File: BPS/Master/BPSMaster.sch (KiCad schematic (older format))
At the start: 21 parts, among them J1 SWD, J12 Logic Analyzer, J13 CAN Analyzer, SW1 B3SL-1002P, U1 STM32F413RHTx, Y1 8M

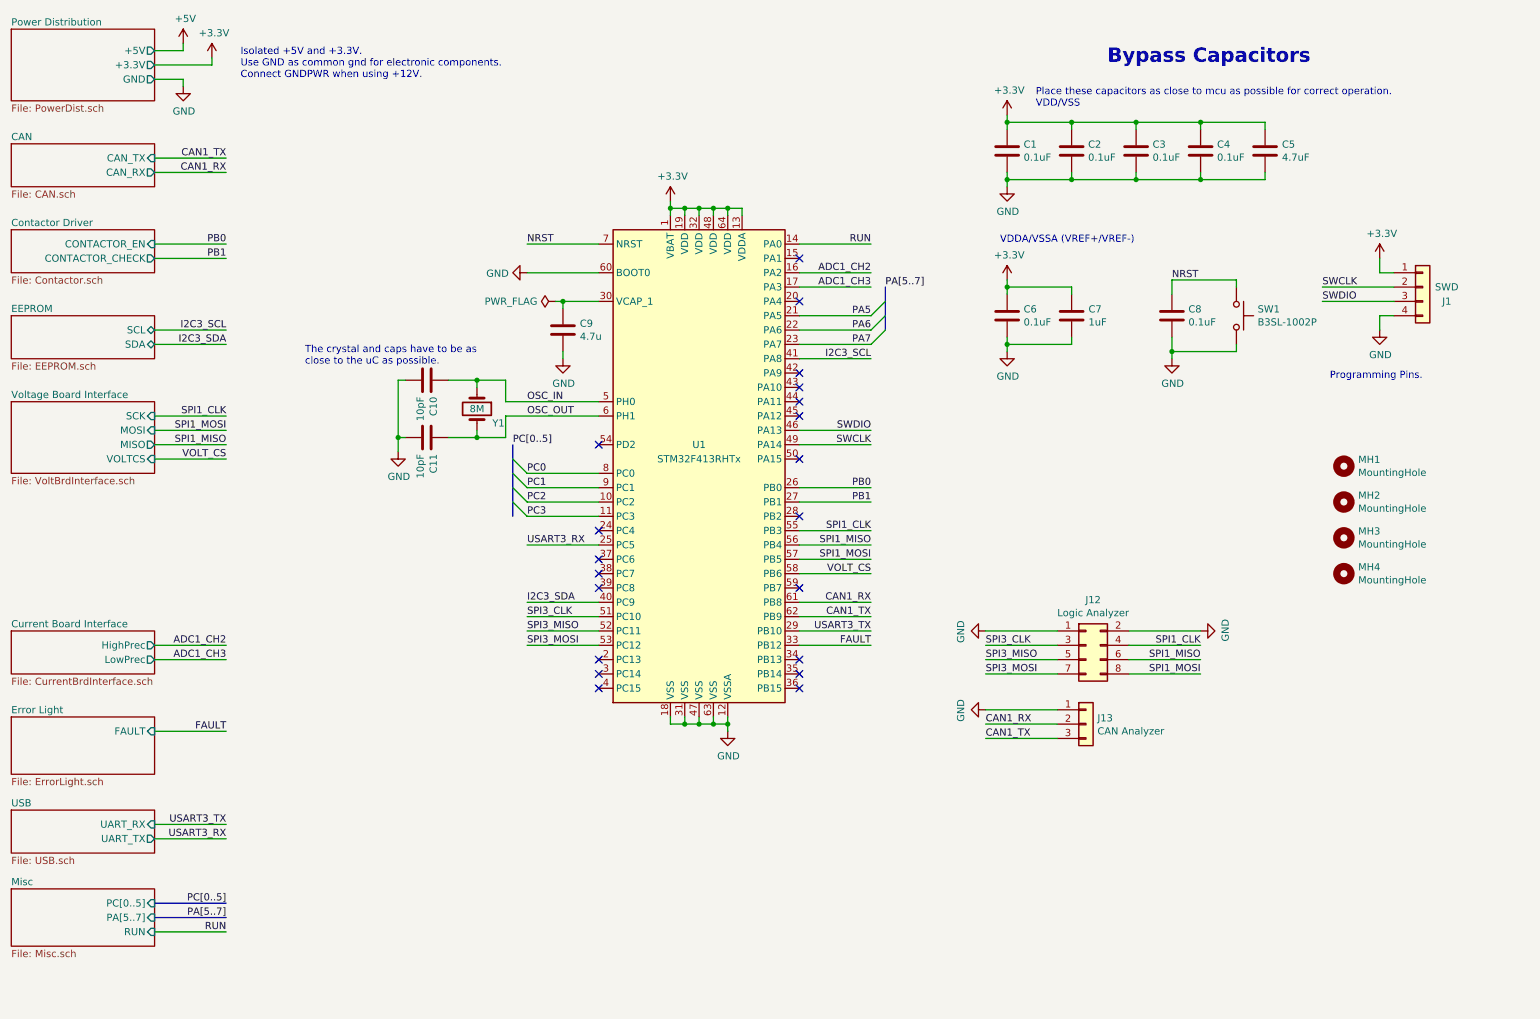
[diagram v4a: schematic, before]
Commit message: Adds BPS master board with no temperature brd electronics and ContactorDriver for dashboard to control.
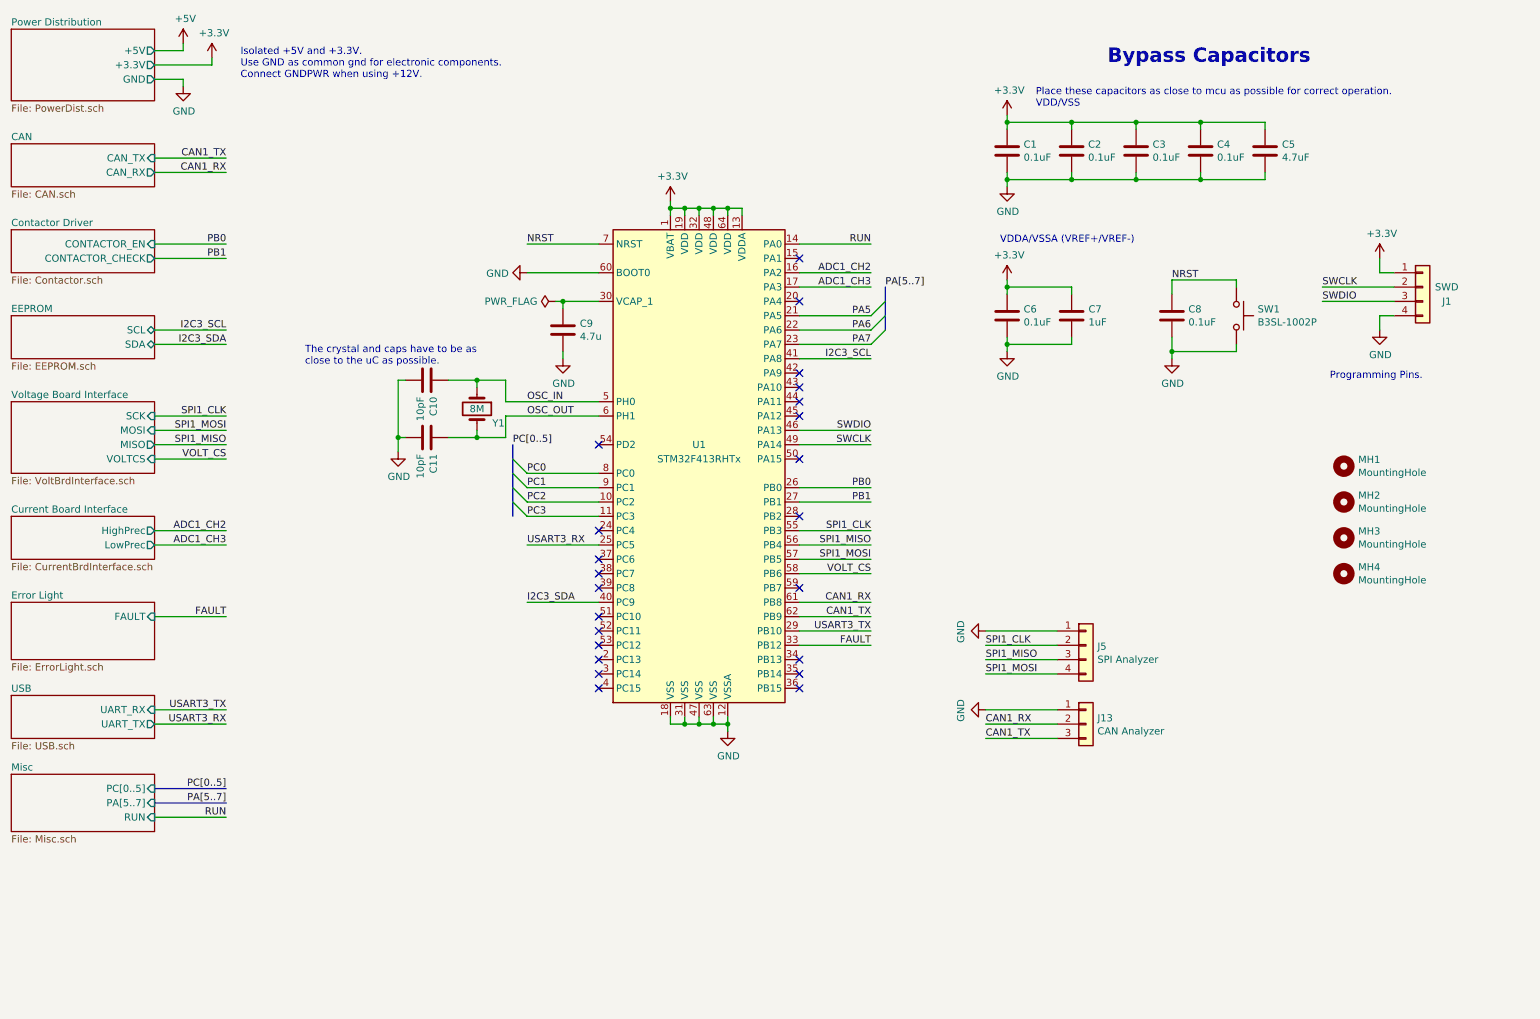
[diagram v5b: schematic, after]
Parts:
- removed J12: Logic Analyzer, Connector_PinHeader_2.54mm:PinHeader_2x04_P2.54mm_Vertical, symbol Connector_Generic:Conn_02x04_Odd_Even
- added J5: SPI Analyzer, Connector_PinHeader_2.54mm:PinHeader_1x04_P2.54mm_Vertical, symbol Connector_Generic:Conn_01x04
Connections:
- net GND: now also J5.1 (Pin_1)
- net SPI1_CLK: now also J5.2 (Pin_2)
- net SPI1_MISO: now also J5.3 (Pin_3)
- net SPI1_MOSI: now also J5.4 (Pin_4)
- net SPI3_CLK: no longer names the net of U1.51 (PC10)
- net SPI3_MISO: no longer names the net of U1.52 (PC11)
- net SPI3_MOSI: no longer names the net of U1.53 (PC12)
- no-connect marks 20 -> 23
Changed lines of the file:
@@
 EESchema Schematic File Version 4
-LIBS:BPSMaster-cache
 EELAYER 30 0
 EELAYER END
@@
 	10550 2900 10650 2900
 $Sheet
-S 1000 6900 1000 400
+S 1000 6100 1000 400
 U 5C392C6A
 F0 "Misc" 50
 F1 "Misc.sch" 50
-F2 "PC[0..5]" I R 2000 7000 50
-F3 "PA[5..7]" I R 2000 7100 50
-F4 "RUN" I R 2000 7200 50
+F2 "PC[0..5]" I R 2000 6200 50
+F3 "PA[5..7]" I R 2000 6300 50
+F4 "RUN" I R 2000 6400 50
 $EndSheet
 Text Notes 8650 1150 0    100  ~ 20
@@
 Text Label 4500 3800 0    50   ~ 0
 PC[0..5]
-Text Label 2500 7000 2    50   ~ 0
+Text Label 2500 6200 2    50   ~ 0
 PC[0..5]
 Wire Wire Line
@@
 PA[5..7]
 Wire Bus Line
-	2000 7000 2500 7000
+	2000 6200 2500 6200
 Wire Bus Line
-	2000 7100 2500 7100
-Text Label 2500 7100 2    50   ~ 0
+	2000 6300 2500 6300
+Text Label 2500 6300 2    50   ~ 0
 PA[5..7]
 $Comp
@@
 FAULT
 Wire Wire Line
-	2000 5800 2500 5800
-Text Label 2500 5800 2    50   ~ 0
+	2000 5000 2500 5000
+Text Label 2500 5000 2    50   ~ 0
 FAULT
 Wire Wire Line
@@
 RUN
 Wire Wire Line
-	2000 7200 2500 7200
-Text Label 2500 7200 2    50   ~ 0
+	2000 6400 2500 6400
+Text Label 2500 6400 2    50   ~ 0
 RUN
 Wire Wire Line
@@
 	10550 2600 10650 2600
 NoConn ~ 6500 4800
-Wire Wire Line
-	5100 5000 4600 5000
-Wire Wire Line
-	4600 5100 5100 5100
-Wire Wire Line
-	5100 5200 4600 5200
-Text Label 4600 5000 0    50   ~ 0
-SPI3_CLK
-Text Label 4600 5100 0    50   ~ 0
-SPI3_MISO
-Text Label 4600 5200 0    50   ~ 0
-SPI3_MOSI
 NoConn ~ 5100 4400
 Wire Wire Line
@@
 $EndSheet
 $Sheet
-S 1000 5700 1000 400
+S 1000 4900 1000 400
 U 5D923D59
 F0 "Error Light" 50
 F1 "ErrorLight.sch" 50
-F2 "FAULT" I R 2000 5800 50
+F2 "FAULT" I R 2000 5000 50
 $EndSheet
 $Sheet
-S 1000 5100 1000 300
+S 1000 4300 1000 300
 U 5D969F1C
 F0 "Current Board Interface" 50
 F1 "CurrentBrdInterface.sch" 50
-F2 "HighPrec" O R 2000 5200 50
-F3 "LowPrec" O R 2000 5300 50
+F2 "HighPrec" O R 2000 4400 50
+F3 "LowPrec" O R 2000 4500 50
 $EndSheet
 Wire Wire Line
-	2000 5200 2500 5200
-Wire Wire Line
-	2000 5300 2500 5300
-Text Label 2500 5200 2    50   ~ 0
+	2000 4400 2500 4400
+Wire Wire Line
+	2000 4500 2500 4500
+Text Label 2500 4400 2    50   ~ 0
 ADC1_CH2
-Text Label 2500 5300 2    50   ~ 0
+Text Label 2500 4500 2    50   ~ 0
 ADC1_CH3
 $Sheet
-S 1000 6350 1000 300
+S 1000 5550 1000 300
 U 5D99F192
 F0 "USB" 50
 F1 "USB.sch" 50
-F2 "UART_RX" I R 2000 6450 50
-F3 "UART_TX" O R 2000 6550 50
+F2 "UART_RX" I R 2000 5650 50
+F3 "UART_TX" O R 2000 5750 50
 $EndSheet
-Text Label 2500 6450 2    50   ~ 0
+Text Label 2500 5650 2    50   ~ 0
 USART3_TX
 Wire Wire Line
-	2000 6450 2500 6450
-Text Label 2500 6550 2    50   ~ 0
+	2000 5650 2500 5650
+Text Label 2500 5750 2    50   ~ 0
 USART3_RX
 Wire Wire Line
-	2000 6550 2500 6550
-Wire Wire Line
-	8800 5200 9300 5200
-Wire Wire Line
-	8800 5300 9300 5300
-Wire Wire Line
-	8800 5400 9300 5400
-Text Label 9300 5200 2    50   ~ 0
-SPI1_CLK
-Text Label 9300 5300 2    50   ~ 0
-SPI1_MISO
-Text Label 9300 5400 2    50   ~ 0
-SPI1_MOSI
-Wire Wire Line
-	8300 5200 7800 5200
-Wire Wire Line
-	7800 5300 8300 5300
-Wire Wire Line
-	8300 5400 7800 5400
-Text Label 7800 5200 0    50   ~ 0
-SPI3_CLK
-Text Label 7800 5300 0    50   ~ 0
-SPI3_MISO
-Text Label 7800 5400 0    50   ~ 0
-SPI3_MOSI
+	2000 5750 2500 5750
 $Comp
 L power:GND #PWR0101
@@
 	7800 5100 8300 5100
 $Comp
-L power:GND #PWR0102
-U 1 1 5D8EC587
-P 9300 5100
-F 0 "#PWR0102" H 9300 4850 50  0001 C CNN
-F 1 "GND" H 9305 4927 50  0000 C CNN
-F 2 "" H 9300 5100 50  0001 C CNN
-F 3 "" H 9300 5100 50  0001 C CNN
-	1    9300 5100
-	0    -1   -1   0
-$EndComp
-Wire Wire Line
-	9300 5100 8800 5100
-$Comp
-L Connector_Generic:Conn_02x04_Odd_Even J12
-U 1 1 5D8D153A
-P 8500 5200
-F 0 "J12" H 8550 5517 50  0000 C CNN
-F 1 "Logic Analyzer" H 8550 5426 50  0000 C CNN
-F 2 "Connector_PinHeader_2.54mm:PinHeader_2x04_P2.54mm_Vertical" H 8500 5200 50  0001 C CNN
-F 3 "~" H 8500 5200 50  0001 C CNN
-	1    8500 5200
-	1    0    0    -1
-$EndComp
-$Comp
 L Connector_Generic:Conn_01x03 J13
 U 1 1 5D9A509E
@@
 NoConn ~ 6500 5400
 NoConn ~ 6500 5500
+$Comp
+L Connector_Generic:Conn_01x04 J5
+U 1 1 5E2EFB22
+P 8500 5200
+F 0 "J5" H 8580 5192 50  0000 L CNN
+F 1 "SPI Analyzer" H 8580 5101 50  0000 L CNN
+F 2 "Connector_PinHeader_2.54mm:PinHeader_1x04_P2.54mm_Vertical" H 8500 5200 50  0001 C CNN
+F 3 "~" H 8500 5200 50  0001 C CNN
+	1    8500 5200
+	1    0    0    -1
+$EndComp
+NoConn ~ 5100 5000
+NoConn ~ 5100 5100
+NoConn ~ 5100 5200
+Wire Wire Line
+	8300 5200 7800 5200
+Wire Wire Line
+	8300 5300 7800 5300
+Wire Wire Line
+	8300 5400 7800 5400
+Text Label 7800 5200 0    50   ~ 0
+SPI1_CLK
+Text Label 7800 5300 0    50   ~ 0
+SPI1_MISO
+Text Label 7800 5400 0    50   ~ 0
+SPI1_MOSI
 Wire Bus Line
 	7100 2700 7100 3000
